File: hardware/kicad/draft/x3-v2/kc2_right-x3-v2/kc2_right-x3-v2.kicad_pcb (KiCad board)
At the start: 2 copper layers, 163.7 x 126.8 mm, 81 parts, among them SW1 KEY_01, SW10 KEY_10, SW11 KEY_11, SW12 KEY_12, SW13 KEY_13, SW14 KEY_14, SW15 KEY_15, SW16 KEY_16, SW17 KEY_17, SW18 KEY_18, SW19 KEY_19, SW2 KEY_02, SW20 KEY_20, SW21 KEY_21, SW22 KEY_22, SW23 KEY_23, SW24 KEY_24, SW25 KEY_25, SW26 KEY_26, SW27 KEY_27, SW28 KEY_28, SW29 KEY_29, SW3 KEY_03, SW30 KEY_30, SW31 KEY_31, SW32 KEY_32, SW33 KEY_33, SW34 KEY_34, SW35 KEY_35, SW36 KEY_36, SW37 KEY_37, SW38 KEY_38, SW39 KEY_39, SW4 KEY_04, SW5 KEY_05, SW6 KEY_06, SW7 KEY_07, SW8 KEY_08, SW9 KEY_09, U1 nice!nano_v2_socket_24pin

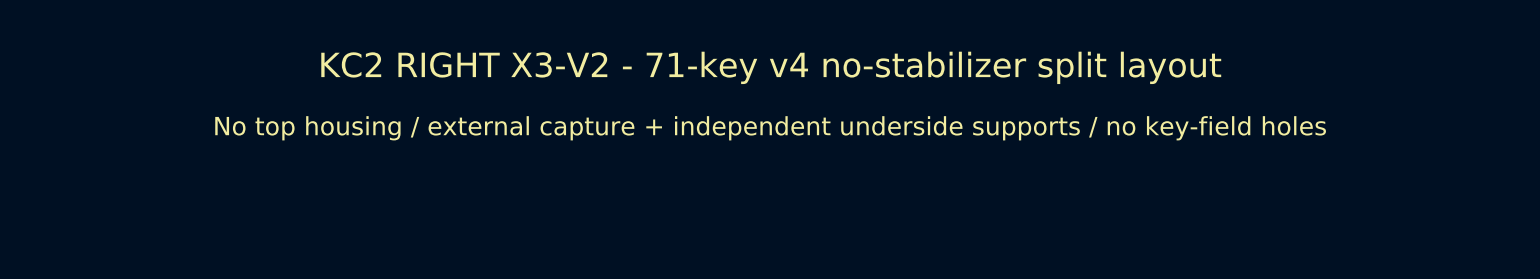
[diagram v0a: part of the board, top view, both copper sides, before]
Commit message: feat(x3-v2): revise left layout to 70-key v5
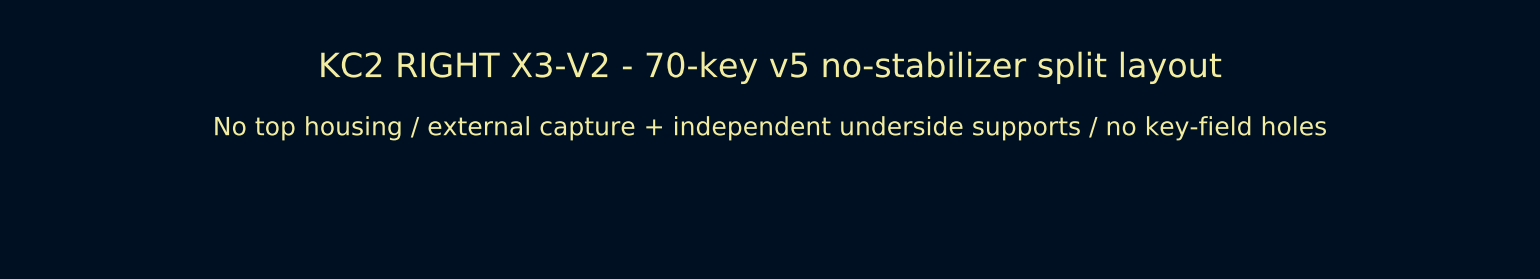
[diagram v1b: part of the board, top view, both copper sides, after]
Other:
- board text added: "KC2 RIGHT X3-V2 - 70-key v5 no-stabilizer split layout"
- board text removed: "KC2 RIGHT X3-V2 - 71-key v4 no-stabilizer split layout"
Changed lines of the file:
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@@
 		)
 	)
-	(gr_text "KC2 RIGHT X3-V2 - 71-key v4 no-stabilizer split layout"
+	(gr_text "KC2 RIGHT X3-V2 - 70-key v5 no-stabilizer split layout"
 		(at 35 24 0)
 		(layer "F.SilkS")

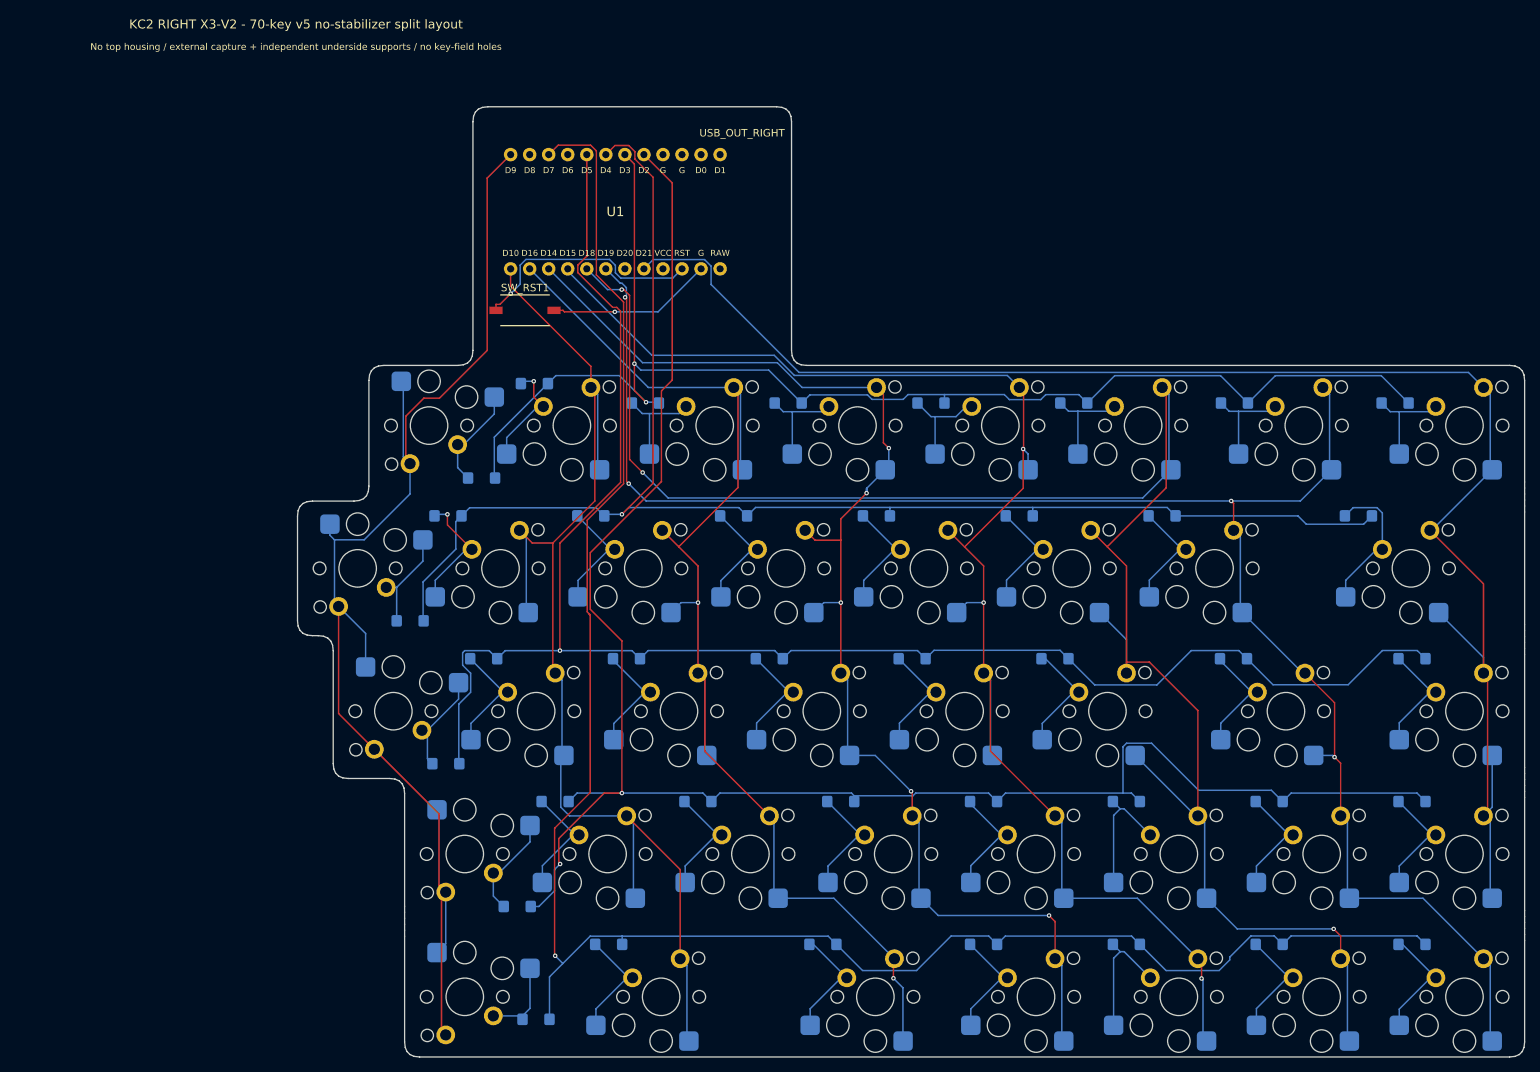
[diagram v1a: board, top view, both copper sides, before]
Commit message: feat(x3-v2): finalize ES1B mounting prototype
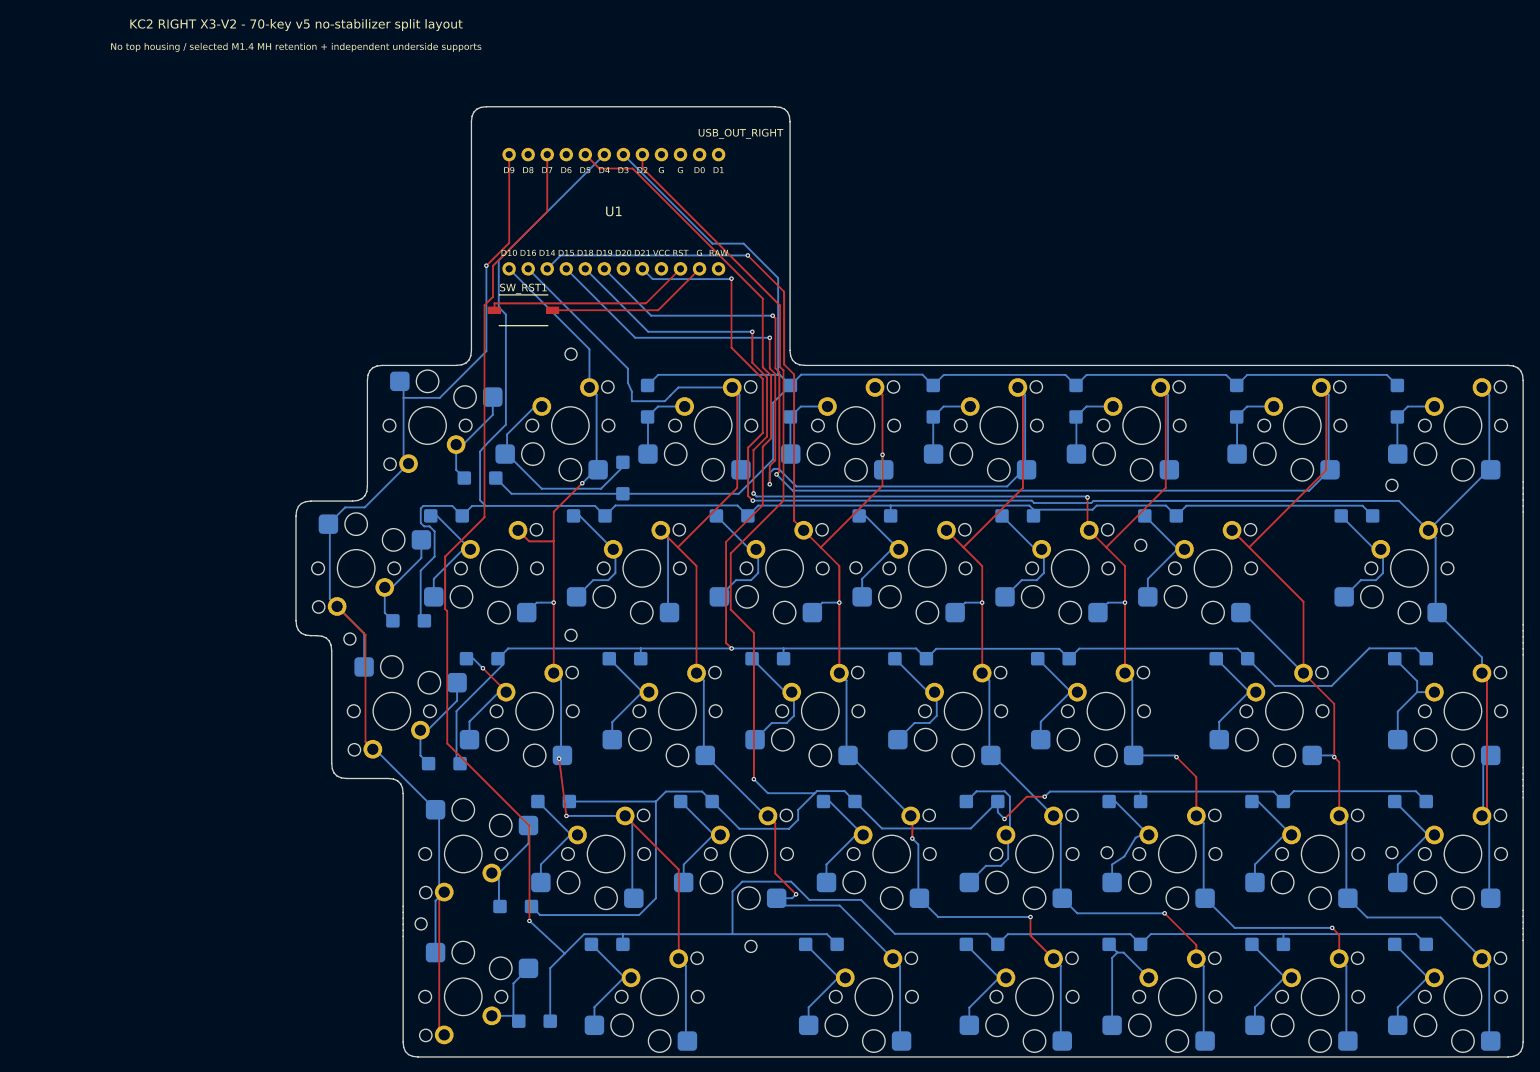
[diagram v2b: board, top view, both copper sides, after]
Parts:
- added MH1: M1.4_NPTH_1.60, MH_M1.4_NPTH_1.60, F.Cu at (71.7, 68.0)
- added MH10: M1.4_NPTH_1.60, MH_M1.4_NPTH_1.60, F.Cu at (95.7, 147.0)
- added MH2: M1.4_NPTH_1.60, MH_M1.4_NPTH_1.60, F.Cu at (181.2, 85.5)
- added MH3: M1.4_NPTH_1.60, MH_M1.4_NPTH_1.60, F.Cu at (147.7, 93.5)
- added MH4: M1.4_NPTH_1.60, MH_M1.4_NPTH_1.60, F.Cu at (109.7, 96.5)
- added MH5: M1.4_NPTH_1.60, MH_M1.4_NPTH_1.60, F.Cu at (71.7, 105.5)
- added MH6: M1.4_NPTH_1.60, MH_M1.4_NPTH_1.60, F.Cu at (42.2, 106.0)
- added MH7: M1.4_NPTH_1.60, MH_M1.4_NPTH_1.60, F.Cu at (181.2, 134.5)
- added MH8: M1.4_NPTH_1.60, MH_M1.4_NPTH_1.60, F.Cu at (143.2, 134.5)
- added MH9: M1.4_NPTH_1.60, MH_M1.4_NPTH_1.60, F.Cu at (51.7, 144.0)
- D1, D10, D11, D12, D13, D14, D15, D16, D17, D18, D19, D2, D20, D21, D22, D23, D24, D25, D26, D27, D28, D29, D3, D30, D31, D32, D33, D34, D35, D36, D37, D38, D39, D4, D5, D6, D7, D8, D9: value 1N4148W_SOD123_DeviceMart_14592018 -> ES1B_Jingdao_C437840_Eleparts9475342; footprint D_SOD123_HandSolder_14592018 -> D_ES1B_SMA_HandSolder_C437840
- moved D2 17.3 mm to (78.6, 84.5), turned to 90 degrees
- moved D3 0.39 mm to (81.9, 74.3), turned to -90 degrees
- moved D6 0.39 mm to (139.1, 74.3), turned to -90 degrees
- moved D7 0.39 mm to (160.5, 74.3), turned to -90 degrees
- moved D4 0.39 mm to (101.0, 74.3), turned to -90 degrees
- moved D5 0.39 mm to (120.0, 74.3), turned to -90 degrees
- moved D8 0.39 mm to (181.9, 74.3), turned to -90 degrees
- moved D33 0.32 mm to (66.8, 157.0)
- moved D15 0.20 mm to (150.3, 89.6)
- moved D22 0.20 mm to (136.0, 108.6)
- moved D23 0.20 mm to (159.8, 108.6)
- moved D24 0.20 mm to (183.7, 108.6)
- moved D32 0.20 mm to (183.7, 127.7)
- moved D39 0.20 mm to (183.7, 146.7)
- moved SW15 0.20 mm to (157.3, 96.6)
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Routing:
- net R_COL6: track 233.3 -> 262.9 mm, vias 4 -> 3
- net R_COL5: track 255.6 -> 232.4 mm, vias 3 -> 6
- net R_COL0: track 181.4 -> 160.0 mm, vias 0 -> 1
- net R_COL4: track 198.6 -> 219.3 mm, vias 3 -> 4
- net R_ROW3: track 246.3 -> 264.8 mm, vias 2 -> 3
- net R_COL1: track 161.8 -> 143.5 mm, vias 0 -> 4
- net R_ROW4: track 257.9 -> 273.9 mm
- net R_ROW0: track 181.2 -> 196.8 mm, vias 2 -> 0
- net R_COL3: track 174.5 -> 188.4 mm
- net RK02_D: track 14.5 -> 28.2 mm, vias 1 -> 0
- net R_ROW1: track 199.3 -> 206.8 mm, vias 1 -> 0
- net RK29_D: track 15.0 -> 21.8 mm
- net R_COL7: track 216.2 -> 222.3 mm, vias 0 -> 2
- net R_ROW2: track 228.8 -> 233.1 mm
- net RST: track 31.7 -> 27.6 mm, vias 1 -> 0
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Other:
- board text added: "Diode: Jingdao ES1B / C437840 / Eleparts 9475342; pad 1 = row cathode"
- board text added: "No top housing / selected M1.4 MH retention + independent underside supports"
- board text removed: "Diode fallback: 1N4148W SOD-123 because DO-35 conflicts with compact hybrid footprint"
- board text removed: "No top housing / external capture + independent underside supports / no key-field holes"

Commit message: feat(x3-v2): compact controller tab and label mounts
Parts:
- moved SW_RST1 29.0 mm to (94.3, 63.5), turned to 90 degrees
- moved BAT_LEAD_SLOT1 1.75 mm to (92.2, 50.8)
- moved U1 1.75 mm to (77.4, 50.8)
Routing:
- net R_ROW3: track 264.8 -> 237.1 mm, vias 3 -> 2
- net R_ROW4: track 273.9 -> 246.9 mm
- net R_COL6: track 262.9 -> 239.4 mm
- net R_COL0: track 160.0 -> 182.5 mm, vias 1 -> 0
- net R_COL2: track 174.6 -> 152.3 mm, vias 1 -> 3
- net R_COL7: track 222.3 -> 202.5 mm, vias 2 -> 0
- net GND: track 21.9 -> 6.10 mm
- net RST: track 27.6 -> 12.8 mm
- net R_COL3: track 188.4 -> 175.9 mm, vias 5 -> 3
- net R_COL5: track 232.4 -> 226.2 mm, vias 6 -> 3
- net RK24_D: track 15.4 -> 21.6 mm
- net RK29_D: track 21.8 -> 16.1 mm
- net RK02_D: track 28.2 -> 24.0 mm
- net R_ROW1: track 206.8 -> 211.0 mm, vias 0 -> 1
- net R_ROW2: track 233.1 -> 229.2 mm, vias 1 -> 2
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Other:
- board size 163.7 x 126.8 mm -> 163.7 x 122.5 mm

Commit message: feat(x3-v2): USB 하부 리셋 배치와 실크 충돌 수정
소켓으로 높아진 nice!nano 아래 공간을 활용하도록 좌우 리셋 배치와 RST/GND 라우팅을 재구성한다. 우측 Reference 필드를 안전한 위치로 옮겨 DRC 경고를 제거하고 SRS, 해시 증거, 생성·검증 코드를 갱신한다.

Requirements: CON-ARCH-004, CON-ARCH-006, OPS-ARCH-003
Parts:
- moved SW_RST1 12.9 mm to (96.3, 50.8)
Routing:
- net GND: track 6.10 -> 14.8 mm, vias 0 -> 2
- net RST: track 12.8 -> 11.2 mm, vias 0 -> 1
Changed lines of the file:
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@@
 	(footprint "SW_NW3_A06_B3_SMD"
 		(layer "F.Cu")
-		(at 94.3 63.45 90)
+		(at 96.35 50.75 90)
 		(descr "Microstack NW3-A06-B3 micro tact switch, SMD, 6.1 x 3.7 mm body, 2.55 mm height, DeviceMart no.1322056")
 		(tags "switch tactile SPST SMD NW3-A06-B3")
 		(property "Reference" "SW_RST1"
-			(at 0 -3 90)
+			(at -7.25 0 0)
 			(layer "F.SilkS")
 			(effects
@@
 	)
 	(segment
-		(start 93.2171 59.7312)
-		(end 90.1912 59.7312)
+		(start 95 52.7)
+		(end 94.1 53.6)
 		(width 0.25)
 		(layer "F.Cu")
@@
 	)
 	(segment
-		(start 90.1912 59.7312)
-		(end 88.83 58.37)
+		(start 96.35 46.875)
+		(end 95 52.7)
 		(width 0.25)
 		(layer "F.Cu")
@@
 	)
 	(segment
-		(start 94.3 59.575)
-		(end 93.3733 59.575)
+		(start 90 55.7)
+		(end 88.83 58.37)
 		(width 0.25)
 		(layer "F.Cu")
 		(net "GND")
 	)
+	(via
+		(at 90 55.7)
+		(size 0.8)
+		(drill 0.4)
+		(layers "F.Cu" "B.Cu")
+		(net "GND")
+	)
+	(via
+		(at 94.1 53.6)
+		(size 0.8)
+		(drill 0.4)
+		(layers "F.Cu" "B.Cu")
+		(net "GND")
+	)
 	(segment
-		(start 93.3733 59.575)
-		(end 93.2171 59.7312)
+		(start 94.1 53.6)
+		(end 90 55.7)
 		(width 0.25)
-		(layer "F.Cu")
+		(layer "B.Cu")
 		(net "GND")
 	)
 	(segment
-		(start 93.3733 65.4533)
-		(end 86.29 58.37)
+		(start 96.35 54.625)
+		(end 93.9 54.7)
 		(width 0.25)
 		(layer "F.Cu")
 		(net "RST")
 	)
+	(via
+		(at 93.9 54.7)
+		(size 0.8)
+		(drill 0.4)
+		(layers "F.Cu" "B.Cu")
+		(net "RST")
+	)
 	(segment
-		(start 94.3 67.325)
-		(end 93.3733 67.325)
+		(start 87.6 57)
+		(end 86.29 58.37)
 		(width 0.25)
-		(layer "F.Cu")
+		(layer "B.Cu")
 		(net "RST")
 	)
 	(segment
-		(start 93.3733 67.325)
-		(end 93.3733 65.4533)
+		(start 93.9 54.7)
+		(end 92.7 55.5)
 		(width 0.25)
-		(layer "F.Cu")
+		(layer "B.Cu")
+		(net "RST")
+	)
+	(segment
+		(start 89.7 56.9)
+		(end 87.6 57)
+		(width 0.25)
+		(layer "B.Cu")
+		(net "RST")
+	)
+	(segment
+		(start 92.7 55.5)
+		(end 89.7 56.9)
+		(width 0.25)
+		(layer "B.Cu")
 		(net "RST")
 	)

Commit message: feat(x3-v2): add switched battery service layout
- Add direct-solder battery power and mirrored power/reset controls.
- Integrate controller-service openings and lower-housing support.
- Regenerate routing, DRC, fabrication, mechanical, render, and model evidence.
- Document protected KiCad mutations and keep physical gates order-blocked.

Refs: CON-ARCH-004
Refs: CON-ARCH-006
Refs: CON-ARCH-007
Refs: REL-ARCH-001
Refs: OPS-ARCH-003
Refs: OPS-ARCH-004
Refs: OPS-ARCH-005
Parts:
- added BAT1: BAT_301230_30x12mm, KC2:BAT_301230_30x12mm, F.Cu at (78.4, 50.8)
- added J_BAT1: BAT_2Pin_PTH_DirectSolder, KC2:BAT_2Pin_PTH_DirectSolder, F.Cu at (94.3, 59.4)
- added SW_PWR1: SW_IMMS_12V_BSI10_THT, KC2:SW_IMMS_12V_BSI10_THT, F.Cu at (94.3, 63.5)
- moved SW_RST1 17.7 mm to (84.0, 63.5), turned to 180 degrees
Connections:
- U1 pad RAW: (no net) -> NN_B+
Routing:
- net NN_B+: track 0.00 -> 17.2 mm
- net GND: track 14.8 -> 31.2 mm, vias 2 -> 1
- net RST: track 11.2 -> 5.55 mm, vias 1 -> 0
- net R_ROW3: track 237.1 -> 242.0 mm
- net BAT+: track 0.00 -> 4.05 mm
- net R_ROW0: track 195.1 -> 198.4 mm, vias 3 -> 5
- net R_COL5: track 226.2 -> 228.6 mm, vias 3 -> 7
- net R_COL3: track 175.9 -> 173.6 mm
- net R_COL2: track 152.3 -> 151.1 mm, vias 3 -> 6
- net R_COL7: track 202.5 -> 201.4 mm, vias 0 -> 2
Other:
- board text added: "+"
- board text added: "BAT STRAIN RELIEF"
- board text added: "ON< >OFF PWR"
- board text added: "RST"
- board text removed: "BAT LEAD EXIT"
- board text removed: "Battery solders directly to nice!nano B+/B-; no carrier power pads"
- board text removed: "TW301525 80mAh"

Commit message: feat(x3-v2): finalize service controls and rounded mounts
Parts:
- moved MH6 41.7 mm to (62.1, 69.3)
- moved MH9 17.9 mm to (66.9, 153.4)
- moved MH3 10.7 mm to (156.2, 87.0)
- moved MH8 8.50 mm to (143.1, 143.0)
- moved MH7 8.50 mm to (181.2, 143.0)
- moved MH4 8.30 mm to (109.7, 104.8)
- moved MH1 0.10 mm to (71.7, 67.9)
- moved MH2 0.10 mm to (181.1, 85.5)
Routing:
- net R_ROW4: track 246.9 -> 248.3 mm, vias 1 -> 3
- net R_ROW2: track 229.2 -> 230.1 mm, vias 2 -> 4
- net R_COL4: track 219.5 -> 220.0 mm
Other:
- board text removed: "+"
